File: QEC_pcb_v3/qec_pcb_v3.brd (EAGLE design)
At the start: 50.8 x 31.1 mm, 15 parts, among them K1 68611114122

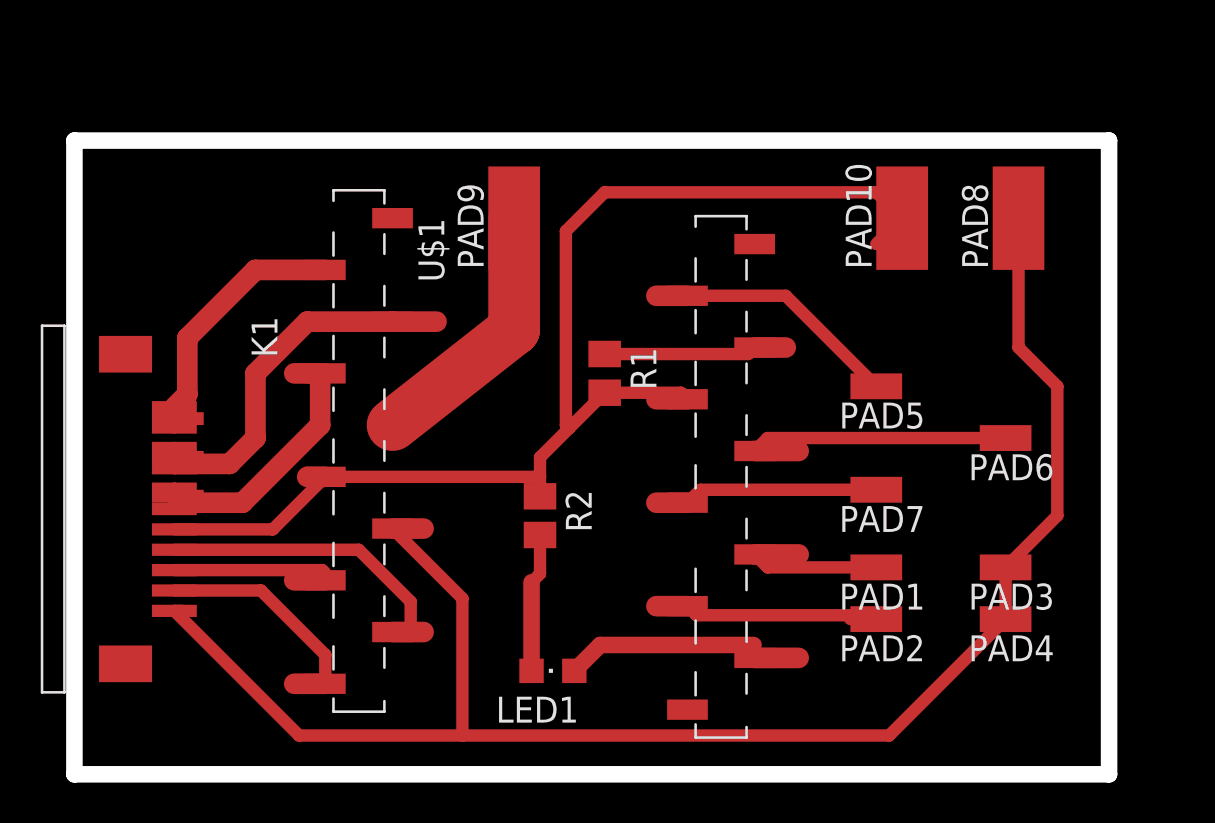
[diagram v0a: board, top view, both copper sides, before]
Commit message: versión 3 control 1 motor
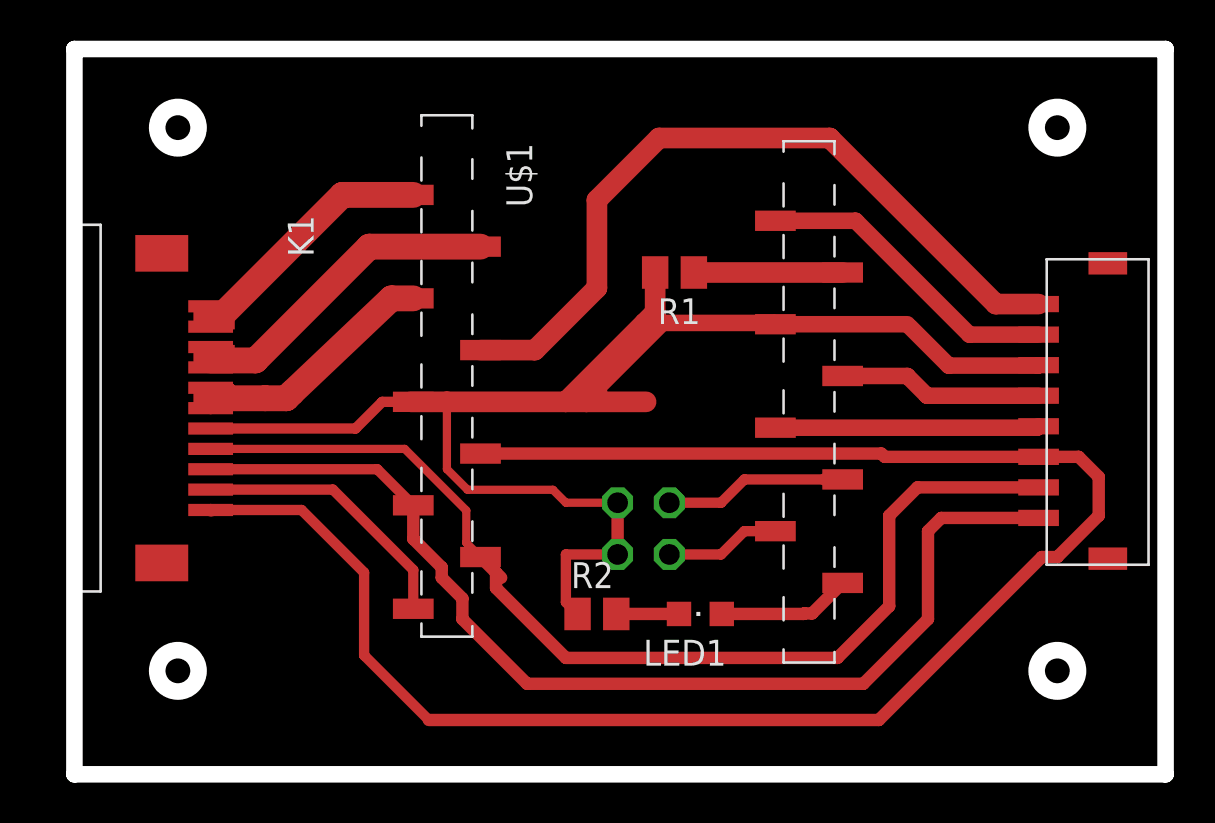
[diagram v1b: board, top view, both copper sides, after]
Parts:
- removed PAD1, PAD2, PAD3, PAD4, PAD5, PAD6, PAD7: (no value), wirepad:SMD1,27-2,54
- removed PAD10, PAD8, PAD9: (no value), wirepad:SMD2,54-5,08
- added CTRL: JST8, dedo:JST
- added JP1: (no value), pinhead:2X02
- R1: value (none) -> 470
- R2: value (none) -> 1k
- moved LED1 7.76 mm to (30.7, 7.87)
- moved R1 6.02 mm to (29.5, 24.6), turned to 180 degrees
- moved U$1 5.68 mm to (27.2, 20.8)
- moved R2 5.58 mm to (25.7, 7.87), turned to 0 degrees
- moved K1 5.26 mm to (5.59, 14.5)
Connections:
- removed net N$10: PAD5.1, U$1.17
- removed net N$13: K1.3, U$1.7
- removed net N$14: K1.4, U$1.8
- removed net N$8: PAD6.1, U$1.14
- removed net N$9: PAD7.1, U$1.13
- new net DIR: CTRL.4, U$1.14
- new net EN: CTRL.5, U$1.13
- new net H1: CTRL.8, K1.3, U$1.7
- new net H2: CTRL.7, K1.4, U$1.8
- new net SVS: CTRL.2, U$1.17
- net +24V: now also CTRL.1; no longer PAD9.1
- net GND: now also CTRL.3, JP1.2, JP1.4; no longer PAD10.1
- net N$3: now also JP1.1, U$1.12; no longer PAD2.1, U$1.11
- net N$4: now also JP1.3, U$1.11; no longer PAD1.1, U$1.12
- net V+: now also CTRL.6; no longer PAD3.1, PAD4.1, PAD8.1
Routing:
- net H1: track 0.00 -> 53.5 mm
- net H2: track 0.00 -> 52.7 mm
- net +24V: track 13.1 -> 37.6 mm
- net GND: track 61.4 -> 82.6 mm
- net N$14: track 16.6 -> 0.00 mm
- net SVS: track 0.00 -> 15.2 mm
- net N$8: track 14.7 -> 0.00 mm
- net EN: track 0.00 -> 12.9 mm
- net N$10: track 12.6 -> 0.00 mm
- net N$9: track 11.1 -> 0.00 mm
- net DIR: track 0.00 -> 10.9 mm
- net N$13: track 9.30 -> 0.00 mm
- net V+: track 80.7 -> 87.2 mm
- net N$2: track 12.1 -> 6.56 mm
- net N$12: track 14.2 -> 18.7 mm
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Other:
- board size 50.8 x 31.1 mm -> 53.6 x 35.6 mm
